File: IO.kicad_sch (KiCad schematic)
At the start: 15 parts, among them P13 14.31818 MHz CLK, U16 74LS32, U17 74LS14, U18 74LS06, U21 74LS00, U25 74LS245, U26 74LS245, U27 74LS245, U28 74LS245, U4 74LS86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

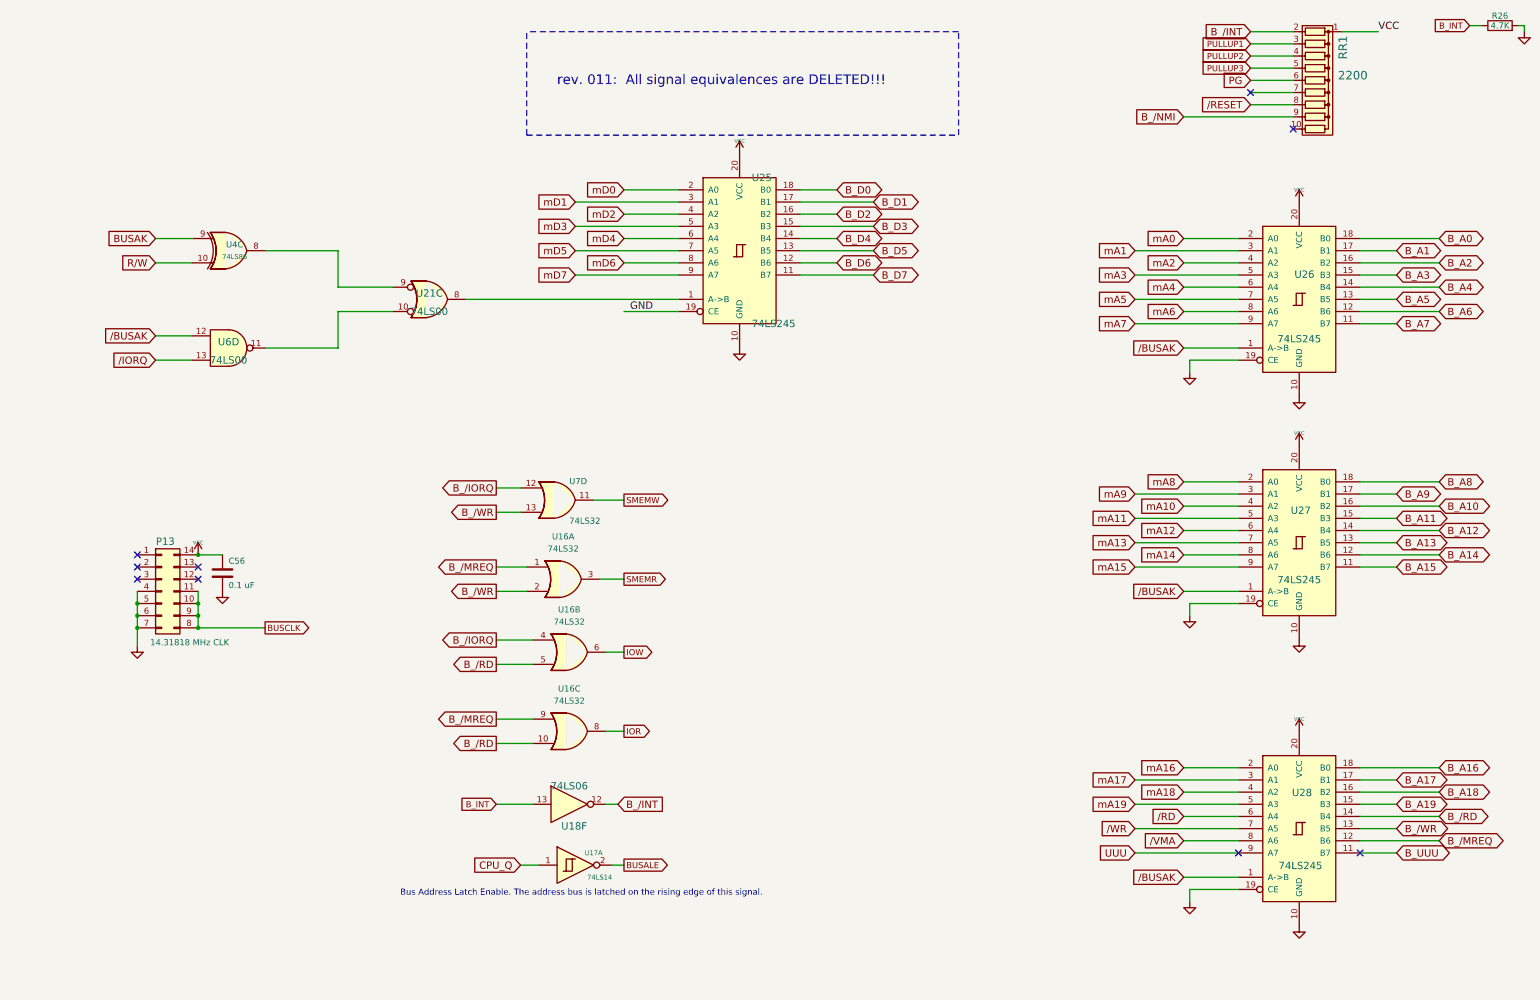
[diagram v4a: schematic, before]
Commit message: fix issue with ISA RW select lines
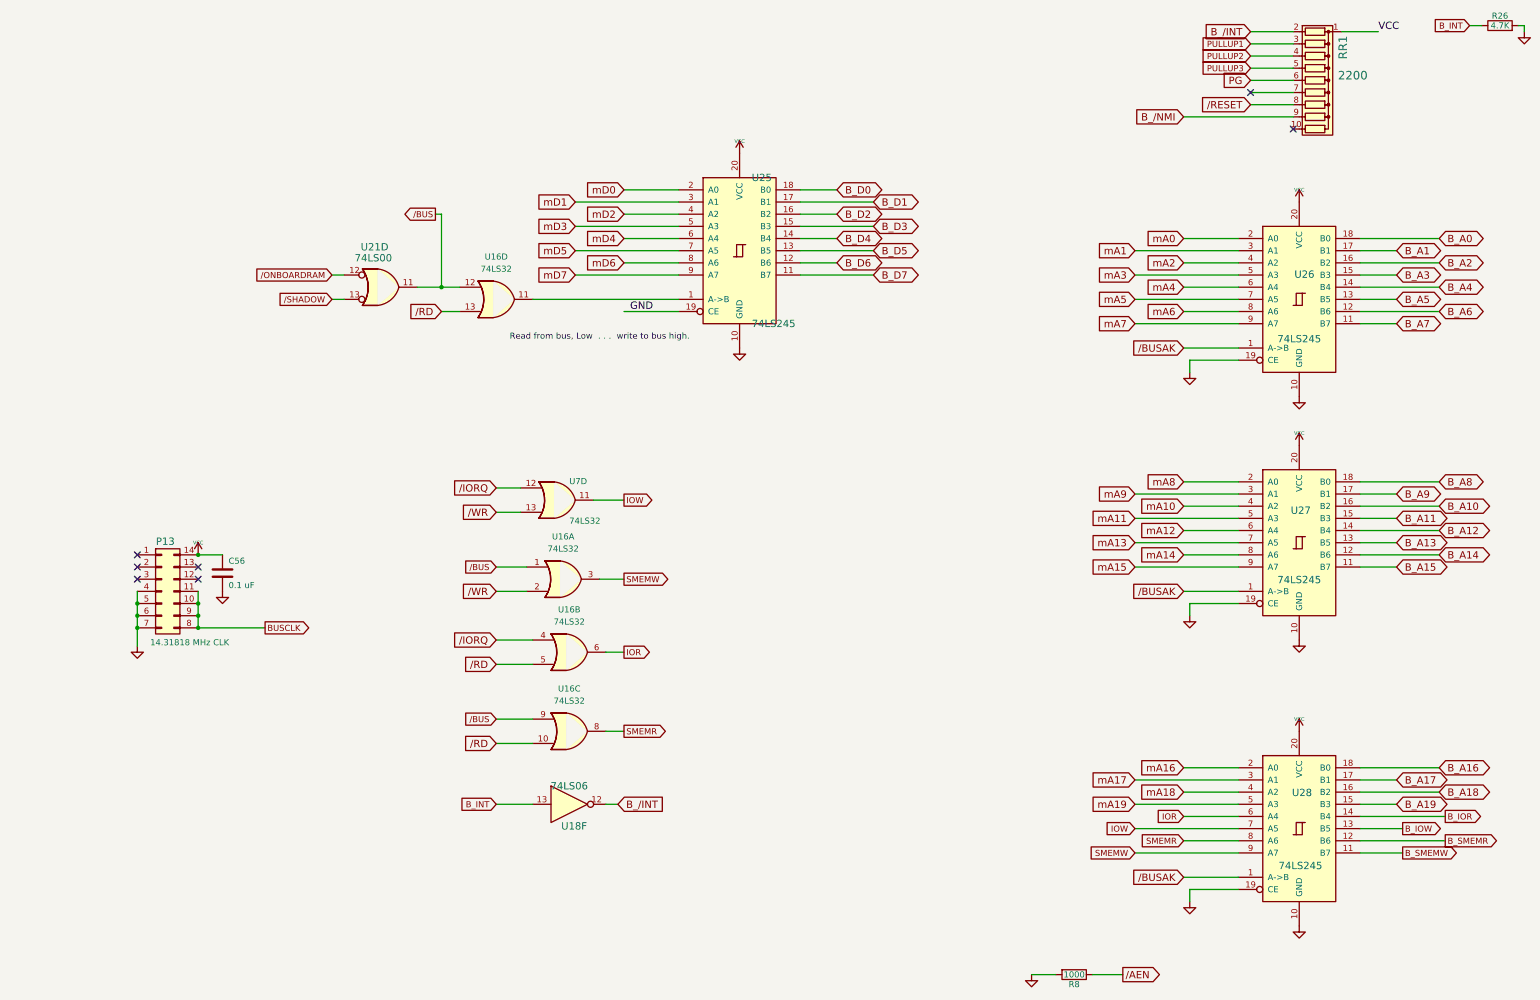
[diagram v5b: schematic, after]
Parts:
- removed U17: 74LS14, Custom:STD_DDW_DIP14, symbol 74xx:74LS14
- removed U21, U6: 74LS00, Custom:STD_DDW_DIP14, symbol 74xx:74LS00
- removed U4: 74LS86, Custom:STD_DDW_DIP14, symbol 74xx:74LS86
- added R8: 1000, Custom:STD_DDW_RESISTOR, symbol Device:R
- added unit 4 of U16
- added U21: 74LS00, Custom:STD_DDW_DIP14, symbol 74xx:74LS00
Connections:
- net /VMA is gone; now on net SMEMR: U28.8 (A6)
- net UUU is gone; now on net SMEMW: U28.9 (A7)
- net /RD: now also U16.10, U16.5, U16.13; no longer U28.6 (A4)
- net /WR: now also U16.2, U7.13; no longer U28.7 (A5)
- net GND: now also R8.2
- net IOR: now also U16.6, U28.6 (A4); no longer U16.8
- net IOW: now also U28.7 (A5), U7.11; no longer U16.6
- net SMEMR: now also U16.8; no longer U16.3
- net SMEMW: now also U16.3; no longer U7.11
- net at U25.1 (A->B): now also U16.11
- net B_/IORQ renamed /IORQ
- net B_/MREQ renamed /BUS
- net /BUS: now also U16.12, U21.11; no longer U28.12 (B6)
- removed net B_/RD: U16.10, U16.5, U28.14 (B4)
- removed net B_/WR: U16.2, U28.13 (B5), U7.13
- net B_UUU renamed B_SMEMW
- new net B_IOR: U28.14 (B4)
- new net B_IOW: U28.13 (B5)
- new net B_SMEMR: U28.12 (B6)
- new net /AEN: R8.1
- new net /ONBOARDRAM: U21.12
- new net /SHADOW: U21.13
- no-connect marks 9 -> 7
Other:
- note added: "Read from bus, Low . . . write to bus high."
- note removed: "Bus Address Latch Enable. The address bus is latched on the rising edge of this signal."
- note removed: "rev. 011: All signal equivalences are DELETED!!!"

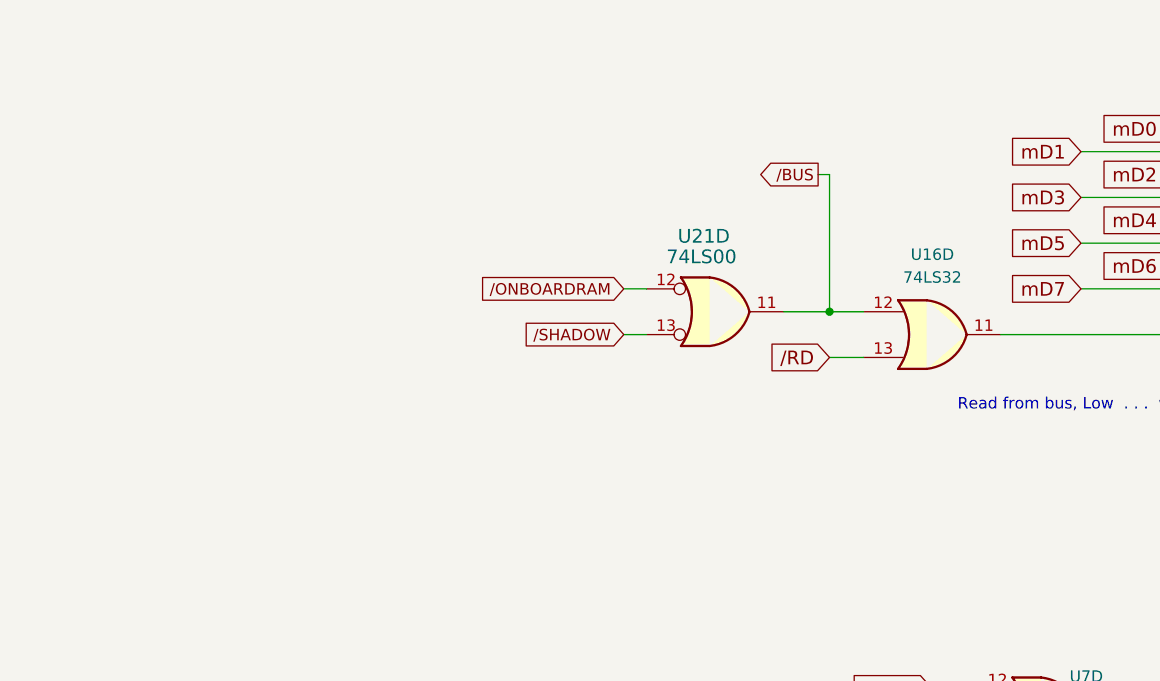
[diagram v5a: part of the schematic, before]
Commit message: fix bus issue
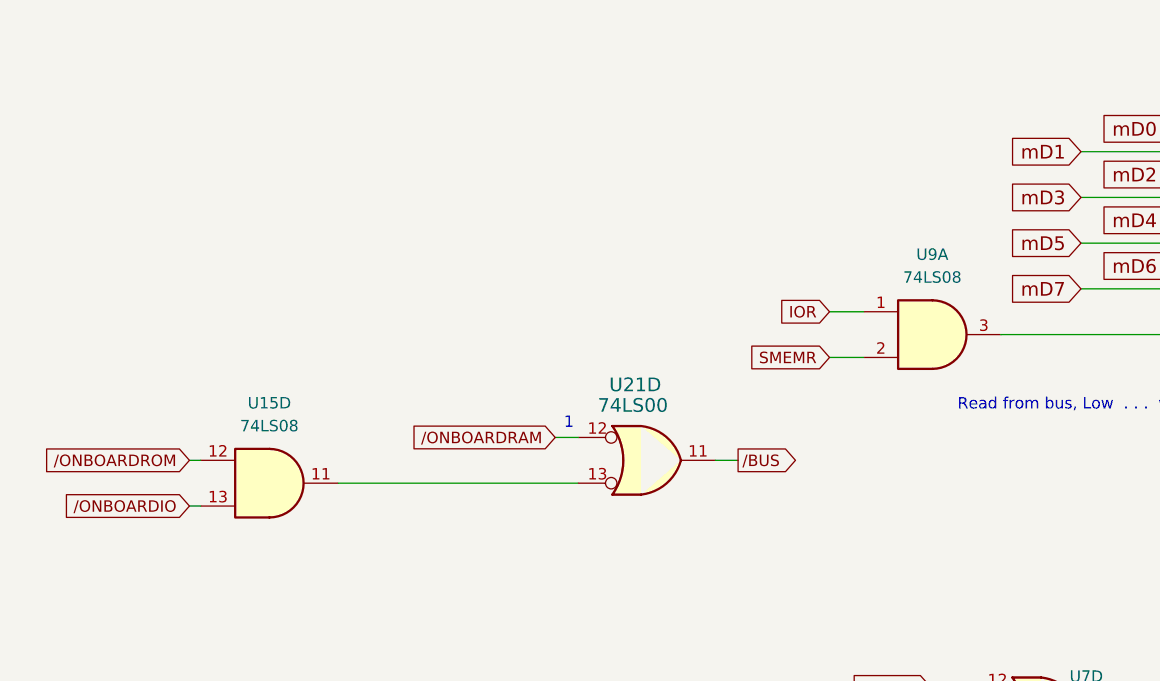
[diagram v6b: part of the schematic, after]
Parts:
- removed unit 4 of U16
- added U15, U9: 74LS08, Custom:STD_DDW_DIP14, symbol 74xx:74LS08
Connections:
- net IOR: now also U9.1
- net SMEMR: now also U9.2
- net at U25.1 (A->B): now also U9.3
- net /SHADOW: no longer names the net of U21.13
- net /SHADOW: now also U15.11
- new net /ONBOARDIO: U15.13
- new net /ONBOARDROM: U15.12
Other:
- note added: "1"
- moved on the sheet: U21D
